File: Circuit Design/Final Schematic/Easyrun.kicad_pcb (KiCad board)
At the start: 2 copper layers, 3 parts, among them U1 ESP32-WROOM-32

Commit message: Footprints
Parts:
- added BProg1: SW_DIP_x02, Button_Switch_SMD:SW_SPST_CK_RS282G05A3, F.Cu at (167.6, 81.3)
- added BRst1: SW_DIP_x01, Button_Switch_SMD:SW_SPST_CK_RS282G05A3, F.Cu at (181.0, 78.7)
- added BT1: Battery_Cell, Battery:BatteryHolder_MPD_BH-18650-PC2, F.Cu at (32.2, 55.2)
- added BT2: Battery_Cell, Battery:BatteryHolder_MPD_BH-18650-PC2, F.Cu at (32.2, 33.7)
- added C1: 100nF, Capacitor_SMD:C_0805_2012Metric_Pad1.18x1.45mm_HandSolder, F.Cu at (164.6, 85.4)
- added C3: 100nF, Capacitor_SMD:C_0805_2012Metric_Pad1.18x1.45mm_HandSolder, F.Cu at (169.4, 85.4)
- added CB1: 100nF, Capacitor_SMD:C_0805_2012Metric_Pad1.18x1.45mm_HandSolder, F.Cu at (188.9, 77.6)
- added CB2: 100nF, Capacitor_SMD:C_0805_2012Metric_Pad1.18x1.45mm_HandSolder, F.Cu at (140.6, 66.5)
- added CB3: 22u, Capacitor_SMD:CP_Elec_6.3x5.8, F.Cu at (108.4, 132.4)
- added CB4: 100nF, Capacitor_SMD:C_0805_2012Metric_Pad1.18x1.45mm_HandSolder, F.Cu at (131.6, 73.9)
- added CB5: 22u, Capacitor_SMD:CP_Elec_6.3x5.8, F.Cu at (135.1, 101.7)
- added CBat1: 10u, Capacitor_SMD:CP_Elec_6.3x5.8, F.Cu at (33.7, 70.1)
- added CBy3: 47u, Capacitor_Tantalum_SMD:CP_EIA-7343-43_Kemet-X_Pad2.25x2.55mm_HandSolder, F.Cu at (118.8, 126.9)
- added CBy5: 47u, Capacitor_Tantalum_SMD:CP_EIA-7343-43_Kemet-X_Pad2.25x2.55mm_HandSolder, F.Cu at (145.5, 96.1)
- added CByBa1: 10u, Capacitor_SMD:CP_Elec_6.3x5.8, F.Cu at (113.1, 27.0)
- added C_by1: 10n, Capacitor_SMD:C_0805_2012Metric_Pad1.18x1.45mm_HandSolder, F.Cu at (30.9, 99.1)
- added C_by_2: C_Polarized, Capacitor_SMD:CP_Elec_6.3x5.8, F.Cu at (74.5, 84.9)
- added C_cv1: 10n, Capacitor_SMD:C_0805_2012Metric_Pad1.18x1.45mm_HandSolder, F.Cu at (35.7, 99.1)
- added Cby2: 0.1u, Capacitor_SMD:C_0805_2012Metric_Pad1.18x1.45mm_HandSolder, F.Cu at (40.5, 99.1)
- added Crec1: 100u, Capacitor_THT:CP_Radial_D6.3mm_P2.50mm, F.Cu at (178.9, 26.8)
- added D1: 1N5822, Diode_THT:D_DO-201AD_P15.24mm_Horizontal, F.Cu at (131.5, 49.8)
- added D2: 1N5822, Diode_THT:D_DO-201AD_P15.24mm_Horizontal, F.Cu at (171.5, 39.8)
- added D3: 1N5822, Diode_THT:D_DO-201AD_P15.24mm_Horizontal, F.Cu at (151.5, 49.8)
- added D4: 1N5822, Diode_THT:D_DO-201AD_P15.24mm_Horizontal, F.Cu at (151.5, 43.0)
- added DB3: 1N5822, Diode_THT:D_DO-201AD_P15.24mm_Horizontal, F.Cu at (85.6, 131.7)
- added DB5: 1N5822, Diode_THT:D_DO-201AD_P15.24mm_Horizontal, F.Cu at (112.3, 101.0)
- added DBoo1: 1N5819, Diode_THT:D_DO-41_SOD81_P10.16mm_Horizontal, F.Cu at (57.3, 83.0)
- added DFly1: 1N5822, Diode_THT:D_DO-201AD_P15.24mm_Horizontal, F.Cu at (158.5, 26.3)
- added D_GREEN1: LED, LED_SMD:LED_0805_2012Metric_Pad1.15x1.40mm_HandSolder, F.Cu at (30.9, 75.7)
- added D_RED1: LED, LED_SMD:LED_0805_2012Metric_Pad1.15x1.40mm_HandSolder, F.Cu at (41.3, 67.5)
- added D_S1: 1N5822, Diode_THT:D_DO-201AD_P15.24mm_Horizontal, F.Cu at (158.5, 33.0)
- added D_S2: 1N5822, Diode_THT:D_DO-201AD_P15.24mm_Horizontal, F.Cu at (131.5, 43.0)
- added FB1: FerriteBead, Resistor_SMD:R_1812_4532Metric_Pad1.30x3.40mm_HandSolder, F.Cu at (132.8, 55.6)
- added J_Display1: Conn_01x09, Connector_JST:JST_EH_S9B-EH_1x09_P2.50mm_Horizontal, F.Cu at (32.0, 112.1)
- added J_I2C1: Conn_01x05_Male, Connector_PinSocket_2.54mm:PinSocket_1x05_P2.54mm_Horizontal, F.Cu at (186.7, 63.6)
- added J_Lector_1: Conn_01x08, Connector_JST:JST_EH_S8B-EH_1x08_P2.50mm_Horizontal, F.Cu at (59.0, 112.1)
- added J_Lector_2: Conn_01x08, Connector_JST:JST_EH_S8B-EH_1x08_P2.50mm_Horizontal, F.Cu at (32.0, 122.5)
- added J_Lector_3: Conn_01x08, Connector_JST:JST_EH_S8B-EH_1x08_P2.50mm_Horizontal, F.Cu at (56.5, 122.5)
- added J_M1: Conn_01x03, Connector_JST:JST_EH_S3B-EH_1x03_P2.50mm_Horizontal, F.Cu at (215.9, 58.4)
- added J_M2: Conn_01x03, Connector_JST:JST_EH_S3B-EH_1x03_P2.50mm_Horizontal, F.Cu at (198.7, 30.6)
- added J_Tap_1: 62409-1, 62409-1_Connector_Faston:TE_62409-1, F.Cu at (193.5, 66.9)
- added J_Tap_2: 62409-1, 62409-1_Connector_Faston:TE_62409-1, F.Cu at (193.5, 63.2)
- added J_Tap_B1: 62409-1, 62409-1_Connector_Faston:TE_62409-1, F.Cu at (133.7, 66.9)
- added J_Tap_B2: 62409-1, 62409-1_Connector_Faston:TE_62409-1, F.Cu at (133.7, 63.2)
- added J_Tap_B3: 62409-1, 62409-1_Connector_Faston:TE_62409-1, F.Cu at (142.7, 63.2)
- added J_Tap_B4: 62409-1, 62409-1_Connector_Faston:TE_62409-1, F.Cu at (133.7, 70.6)
- added J_gnd1: 62409-1, 62409-1_Connector_Faston:TE_62409-1, F.Cu at (177.6, 83.1)
- added J_prog1: Conn_01x06_Male, Connector_PinHeader_2.54mm:PinHeader_1x06_P2.54mm_Horizontal, F.Cu at (164.5, 63.7)
- added LB3: 100u, Inductor_THT:L_Toroid_Vertical_L25.4mm_W14.7mm_P12.20mm_Vishay_TJ5_BigPads, F.Cu at (96.7, 113.9)
- added LB5: 100u, Inductor_THT:L_Toroid_Vertical_L25.4mm_W14.7mm_P12.20mm_Vishay_TJ5_BigPads, F.Cu at (123.4, 83.1)
- added LProg1: LED, LED_SMD:LED_0805_2012Metric_Pad1.15x1.40mm_HandSolder, F.Cu at (191.4, 70.3)
- added Lb1: L, Inductor_THT:L_Toroid_Vertical_L25.4mm_W14.7mm_P12.20mm_Vishay_TJ5_BigPads, F.Cu at (41.9, 83.1)
- added Lrec1: 440m, Inductor_THT:L_Toroid_Vertical_L25.4mm_W14.7mm_P12.20mm_Vishay_TJ5_BigPads, F.Cu at (142.6, 25.2)
- added Qb1: IRF740, Package_TO_SOT_THT:TO-220-3_Vertical, F.Cu at (58.6, 89.0)
- added R1: 10K, Resistor_SMD:R_0805_2012Metric_Pad1.20x1.40mm_HandSolder, F.Cu at (184.5, 82.7)
- added R4: 10K, Resistor_SMD:R_0805_2012Metric_Pad1.20x1.40mm_HandSolder, F.Cu at (200.4, 62.8)
- added R5: 220, Resistor_SMD:R_0805_2012Metric_Pad1.20x1.40mm_HandSolder, F.Cu at (193.7, 76.2)
- added R6: 220, Resistor_SMD:R_0805_2012Metric_Pad1.20x1.40mm_HandSolder, F.Cu at (200.4, 65.8)
- added RB1: 10K, Resistor_SMD:R_0805_2012Metric_Pad1.20x1.40mm_HandSolder, F.Cu at (149.6, 62.8)
- added RB2: 10K, Resistor_SMD:R_0805_2012Metric_Pad1.20x1.40mm_HandSolder, F.Cu at (136.3, 73.9)
- added RI2C1: 10k, Resistor_SMD:R_0805_2012Metric_Pad1.20x1.40mm_HandSolder, F.Cu at (205.1, 62.8)
- added RI2C2: 10k, Resistor_SMD:R_0805_2012Metric_Pad1.20x1.40mm_HandSolder, F.Cu at (196.1, 73.2)
- added RMISO1: 10k, Resistor_SMD:R_0805_2012Metric_Pad1.20x1.40mm_HandSolder, F.Cu at (191.3, 73.2)
- added R_GREEN1: 1k, Resistor_SMD:R_0805_2012Metric_Pad1.20x1.40mm_HandSolder, F.Cu at (46.1, 67.5)
- added R_Prog1: 10k, Resistor_SMD:R_0805_2012Metric_Pad1.20x1.40mm_HandSolder, F.Cu at (120.7, 24.4)
- added R_RED1: 1k, Resistor_SMD:R_0805_2012Metric_Pad1.20x1.40mm_HandSolder, F.Cu at (35.6, 75.6)
- added R_prog1: 47, Resistor_SMD:R_0805_2012Metric_Pad1.20x1.40mm_HandSolder, F.Cu at (196.1, 70.2)
- added Ra1: 47, Resistor_SMD:R_0805_2012Metric_Pad1.20x1.40mm_HandSolder, F.Cu at (54.8, 99.1)
- added Rb1: 100, Resistor_SMD:R_0805_2012Metric_Pad1.20x1.40mm_HandSolder, F.Cu at (50.0, 99.1)
- added Ro1: 1k, Resistor_SMD:R_0805_2012Metric_Pad1.20x1.40mm_HandSolder, F.Cu at (45.3, 99.1)
- added SWRec1: SW_DIP_x01, Connector_PinHeader_2.54mm:PinHeader_1x02_P2.54mm_Vertical_SMD_Pin1Left, F.Cu at (173.1, 46.7)
- added UB3v3: LM2576S-5, Package_TO_SOT_SMD:TO-263-5_TabPin3, F.Cu at (119.0, 117.8)
- added UB5v0: LM2576S-5, Package_TO_SOT_SMD:TO-263-5_TabPin3, F.Cu at (145.7, 87.0)
- added U_555: LM555xM, Package_SO:SOIC-8_3.9x4.9mm_P1.27mm, F.Cu at (59.6, 94.3)
- added U_ChargeControler1: TP4056, TP4056_Bcharge:SOP127P600X175-9N, F.Cu at (113.1, 34.4)
- moved U1 59.4 mm to (193.0, 139.9)
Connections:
- net CS_Lector1 renamed /CS_Lector_1
- U1 pad 10: Butt_No_D -> /Butt_No_D
- U1 pad 11: Butt_D -> /Butt_D
- U1 pad 12: Rst_2 -> /Rst_2
- U1 pad 13: CS_Lector3 -> /CS_Lector3
- U1 pad 16: IO13 -> /IO13
- U1 pad 2: Net-(C_Bypass1-Pad2) -> +3V3
- U1 pad 23: CS_Display -> /CS_Display
- U1 pad 25: Net-(C2-Pad2) -> /IO0
- U1 pad 26: Rst_1 -> /Rst_1
- U1 pad 27: PWM_M1 -> /PWM_M1
- U1 pad 28: PWM_M2 -> /PWM_M2
- U1 pad 3: Net-(C1-Pad1) -> /En
- U1 pad 30: SCK -> /SCK
- U1 pad 31: MISO -> /MISO
- U1 pad 33: Rst_3 -> /Rst_3
- U1 pad 34: Prog_Tx -> /Prog_Tx
- U1 pad 35: Prog_Rx -> /Prog_Rx
- U1 pad 36: CS_Lector2 -> /CS_Lector2
- U1 pad 37: MOSI -> /MOSI
- U1 pad 6: Rst_D -> /Rst_D
- U1 pad 7: D/C -> /D/C
- U1 pad 8: I2C1 -> /I2C1
- U1 pad 9: I2C2 -> /I2C2

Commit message: Organización PCB
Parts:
- removed Display1: Conn_01x04_Female, Connector_PinSocket_2.54mm:PinSocket_1x04_P2.54mm_Vertical
- removed Display_1: Conn_01x14_Female, Connector_PinSocket_2.54mm:PinSocket_1x14_P2.54mm_Vertical
- BT1, BT2, Lrec1: moved to B.Cu
- Lb1: value L -> 100u; moved to B.Cu
- moved U1 184.6 mm to (35.7, 43.2), turned to 90 degrees
- moved J_Tap_2 177.8 mm to (18.5, 95.0), turned to 90 degrees
- moved J_Tap_1 171.8 mm to (25.5, 103.0), turned to 90 degrees
- moved RI2C1 167.0 mm to (38.1, 63.0), turned to -90 degrees
- moved CB1 159.9 mm to (30.5, 55.9), turned to 180 degrees
- moved RI2C2 158.1 mm to (38.1, 68.1), turned to 90 degrees
- moved J_Lector_2 155.1 mm to (154.9, 27.9), turned to -90 degrees
- moved J_I2C1 154.4 mm to (32.3, 66.0)
- moved RMISO1 152.8 mm to (44.5, 31.0)
- moved J_gnd1 152.1 mm to (25.5, 86.5), turned to 90 degrees
- moved R_prog1 147.4 mm to (51.0, 44.6), turned to 180 degrees
- moved LProg1 138.3 mm to (55.5, 44.6), turned to 180 degrees
- moved R4 138.2 mm to (66.0, 30.5), turned to 180 degrees
- moved J_Display1 136.3 mm to (154.9, 53.4), turned to -90 degrees
- moved R6 136.2 mm to (64.5, 55.9), turned to 90 degrees
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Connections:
- DBoo1 pad 2: Net-(Qb1-Pad2) -> Net-(Lb1-Pad2)
- Lb1 pad 2: unconnected-(Lb1-Pad2) -> Net-(Lb1-Pad2)
- Qb1 pad 2: Net-(Qb1-Pad2) -> Net-(Lb1-Pad2)

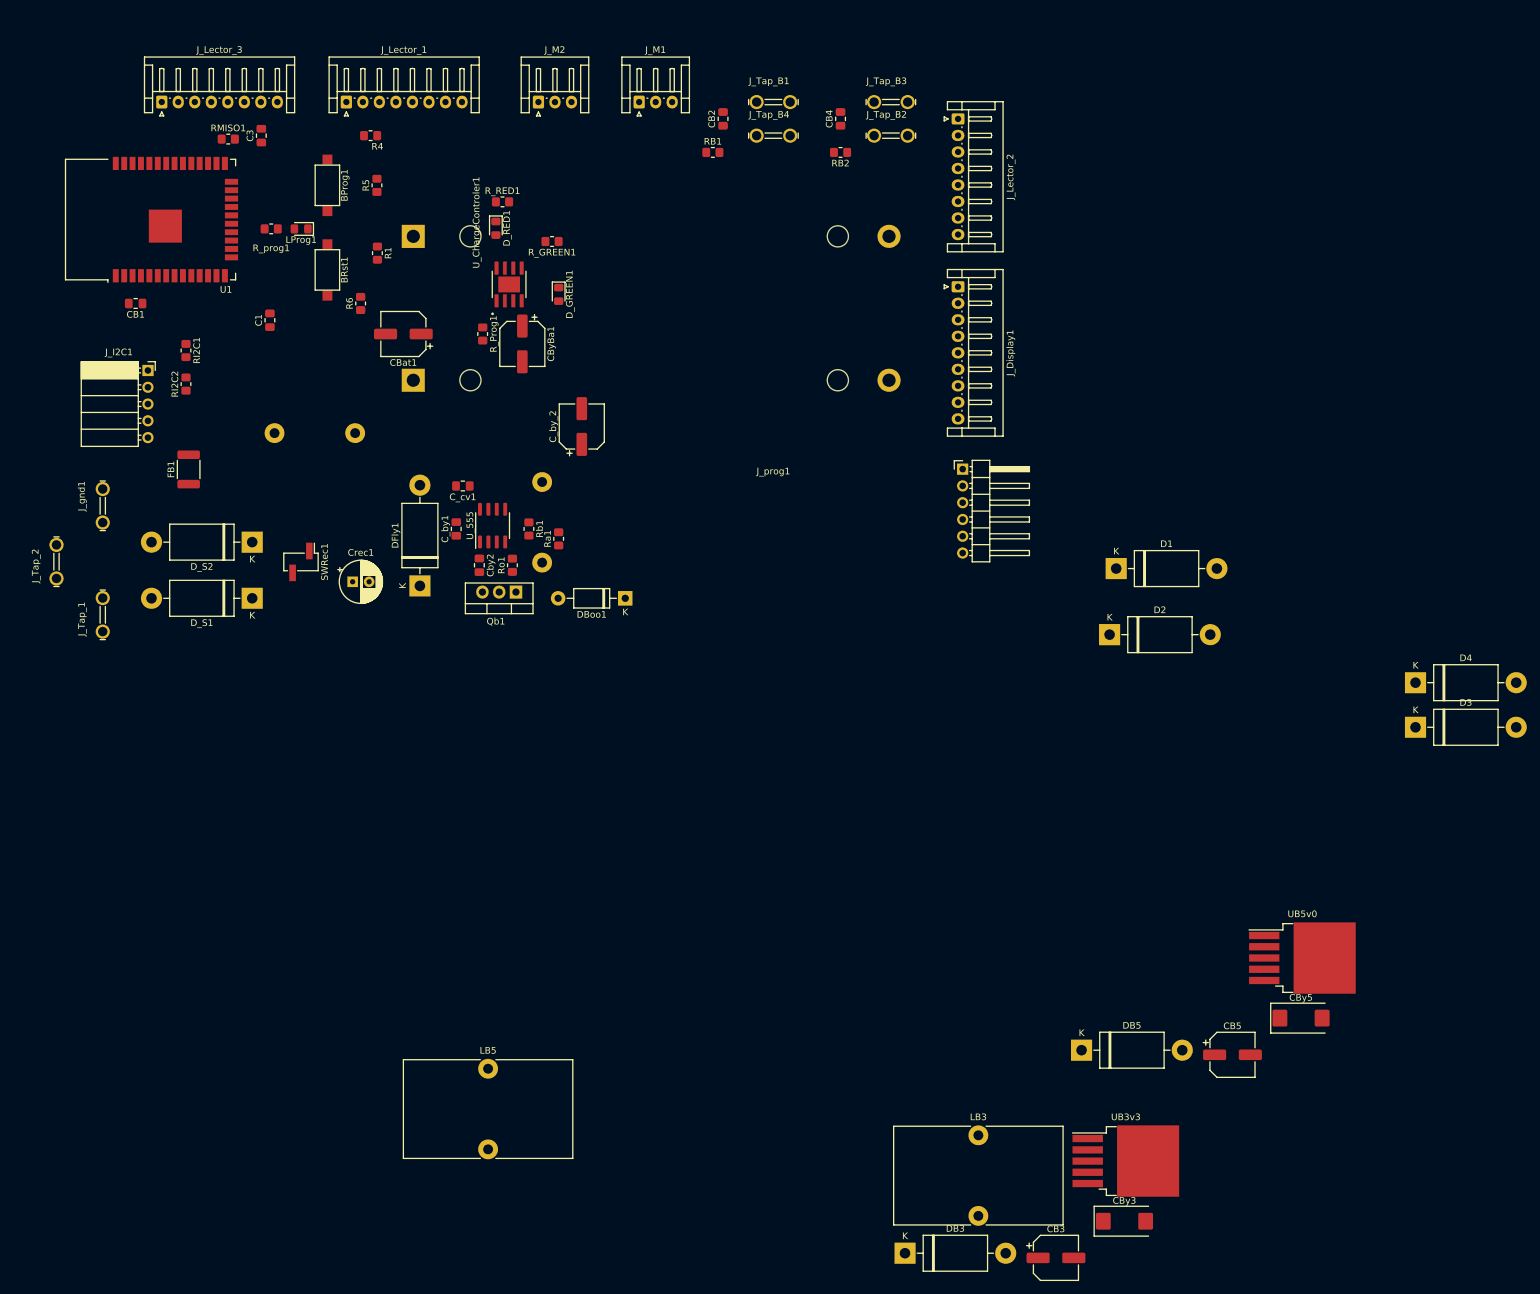
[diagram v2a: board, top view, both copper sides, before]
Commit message: Organización de PCB 2.0
Se organizaron los componentes de la PCB
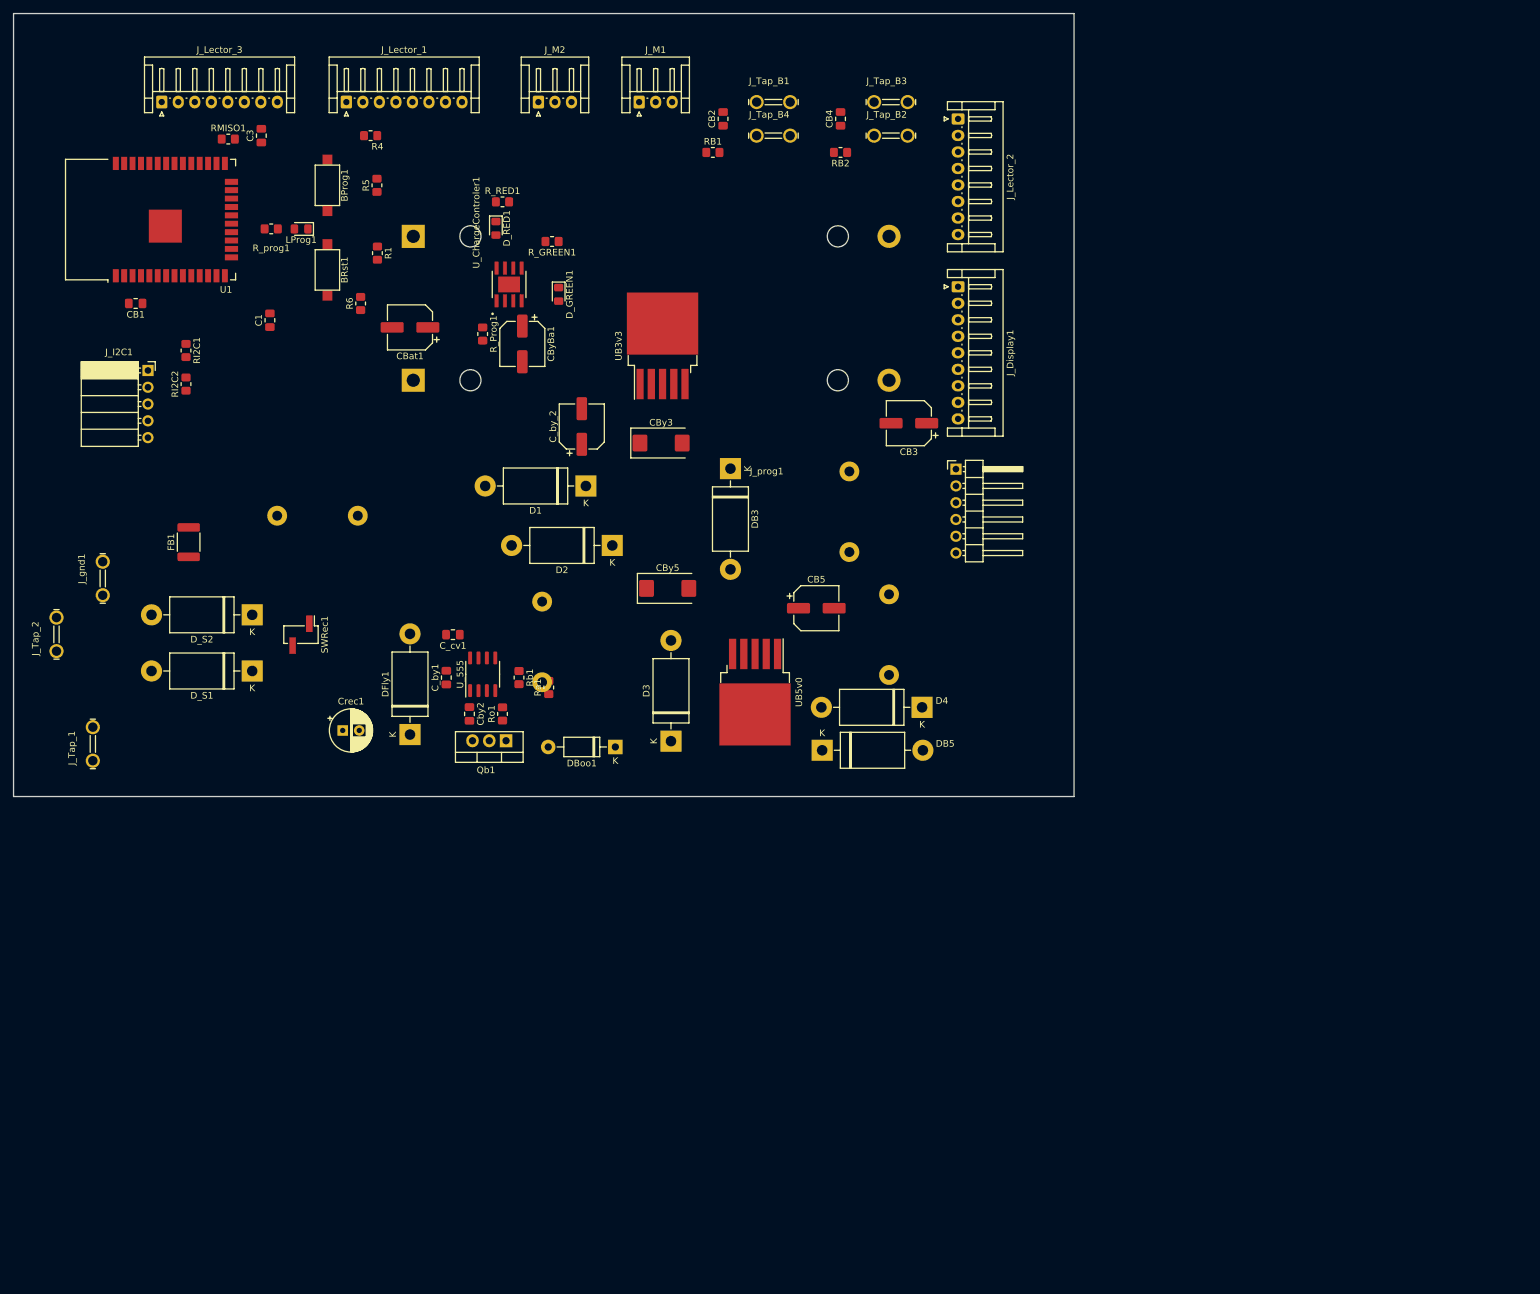
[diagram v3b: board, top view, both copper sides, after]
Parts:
- LB3, LB5: moved to B.Cu
- moved UB3v3 141.9 mm to (110.2, 62.3), turned to 90 degrees
- moved CBy3 137.1 mm to (110.0, 77.0)
- moved CB3 128.3 mm to (147.5, 74.0), turned to 180 degrees
- moved DB3 121.6 mm to (120.5, 80.9), turned to -90 degrees
- moved CBy5 115.8 mm to (111.0, 99.0)
- moved D3 112.7 mm to (111.5, 122.1), turned to 90 degrees
- moved CB5 92.4 mm to (133.5, 102.0)
- moved UB5v0 92.1 mm to (124.2, 114.7), turned to -90 degrees
- moved LB3 90.4 mm to (138.5, 93.5)
- moved D4 90.4 mm to (134.4, 123.5)
- moved LB5 85.1 mm to (144.5, 112.1)
- moved D1 81.2 mm to (98.6, 83.5), turned to 180 degrees
- moved D2 76.5 mm to (102.6, 92.5), turned to 180 degrees
- moved DB5 57.2 mm to (149.5, 117.0), turned to 180 degrees
- moved C_by1 22.5 mm to (77.5, 112.5)
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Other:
- board outline added: 160.5 x 118.5 mm

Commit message: Mejor ruteo xd Felipe cambie las huellas
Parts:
- removed BT2: Battery_Cell, Battery:BatteryHolder_MPD_BH-18650-PC2
- CB5, CBy5, CByBa1, SWRec1: moved to B.Cu
- LB3, LB5, Lb1, Lrec1: moved to F.Cu
- moved J_I2C1 222.1 mm to (249.3, 113.5)
- moved D1 182.2 mm to (275.3, 127.8)
- moved D2 173.1 mm to (267.5, 145.3)
- moved Crec1 161.7 mm to (223.4, 112.3)
- moved Qb1 146.5 mm to (232.9, 116.4)
- moved C_by1 144.5 mm to (218.9, 82.8)
- moved J_gnd1 142.9 mm to (166.1, 122.9), turned to 180 degrees
- moved J_Tap_2 142.0 mm to (160.0, 117.3), turned to 180 degrees
- moved Lb1 139.7 mm to (230.9, 86.4), turned to 0 degrees
- moved Cby2 138.2 mm to (219.2, 118.9)
- moved C_cv1 136.8 mm to (214.9, 95.8)
- moved J_Tap_1 135.9 mm to (159.8, 128.5), turned to 180 degrees
- moved Ro1 133.5 mm to (213.6, 157.2)
- moved U_555 132.6 mm to (215.5, 107.3)
- moved FB1 131.6 mm to (168.9, 109.5)
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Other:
- board size 160.5 x 118.5 mm -> 100 x 100 mm

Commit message: PCB distribution
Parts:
- CByBa1: moved to F.Cu
- C_b1: renamed from C_by_2; moved to B.Cu
- D1, D2, D3, D4, DB3, DB5, DFly1, D_S1, D_S2: footprint Diode_THT:D_DO-201AD_P15.24mm_Horizontal -> Diode_THT:D_DO-201AE_P5.08mm_Vertical_AnodeUp
- DBoo1: footprint Diode_THT:D_DO-41_SOD81_P10.16mm_Horizontal -> Diode_THT:D_DO-201AE_P5.08mm_Vertical_AnodeUp
- J_I2C1: moved to B.Cu
- moved D1 181.6 mm to (96.2, 98.3), turned to -90 degrees
- moved DBoo1 156.8 mm to (78.1, 98.6), turned to -90 degrees
- moved Lb1 150.5 mm to (85.5, 125.4)
- moved D3 144.9 mm to (87.3, 98.4), turned to -90 degrees
- moved D2 139.1 mm to (135.0, 102.9), turned to 0 degrees
- moved Qb1 129.8 mm to (104.8, 95.6), turned to 0 degrees
- moved Ro1 127.3 mm to (113.6, 78.5), turned to 180 degrees
- moved CBy3 119.6 mm to (121.5, 117.4), turned to 180 degrees
- moved Ra1 111.3 mm to (120.2, 78.6), turned to 0 degrees
- moved C_by1 108.8 mm to (110.2, 84.4), turned to -90 degrees
- moved U_555 101.3 mm to (116.9, 84.3), turned to 0 degrees
- moved Cby2 101.2 mm to (123.5, 86.1), turned to 0 degrees
- moved C_cv1 98.4 mm to (116.7, 90.2)
- moved D4 96.7 mm to (105.4, 102.7)
- moved UB3v3 91.5 mm to (123.2, 106.0), turned to 0 degrees
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- renumbered LProg1 to L_p1, R_prog1 to R_p1

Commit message: More free space schematic
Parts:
- CB3: moved to B.Cu
- J_I2C1: moved to F.Cu
- moved CB3 65.9 mm to (92.5, 107.2), turned to 0 degrees
- moved J_Tap_B1 58.7 mm to (90.4, 85.6), turned to 180 degrees
- moved J_Tap_B4 55.8 mm to (90.5, 79.2), turned to 180 degrees
- moved C_by1 50.4 mm to (157.5, 101.9), turned to 90 degrees
- moved Ra1 50.2 mm to (167.9, 94.5)
- moved C_cv1 49.6 mm to (164.6, 102.9)
- moved U_555 48.7 mm to (163.5, 98.4)
- moved Rb1 48.2 mm to (168.9, 98.0), turned to -90 degrees
- moved Cby2 48.2 mm to (168.9, 102.1), turned to -90 degrees
- moved J_Tap_B2 48.0 mm to (105.3, 85.8), turned to 180 degrees
- moved Ro1 48.0 mm to (157.5, 97.8), turned to 90 degrees
- moved J_Tap_B3 47.0 mm to (105.6, 79.2), turned to 180 degrees
- moved CB2 45.7 mm to (97.0, 85.6), turned to 0 degrees
- moved RB1 41.9 mm to (97.0, 79.2), turned to 180 degrees
- moved CB4 36.9 mm to (112.3, 85.8), turned to 0 degrees
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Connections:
- D_RED1 pad 2: Net-(D_RED1-Pad2) -> /PowerModule/Buck5v0
- U1 pad 13: /CS_Lector3 -> CHRG
- U1 pad 14: unconnected-(U1-Pad14) -> STDBY
- U1 pad 24: unconnected-(U1-Pad24) -> /CS_Lector3
- U_ChargeControler1 pad 8: Net-(D_RED1-Pad2) -> /PowerModule/Buck5v0
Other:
- board size 100 x 100 mm -> 100 x 93.1 mm
